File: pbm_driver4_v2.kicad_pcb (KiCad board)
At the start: 4 copper layers, 30 x 70 mm, 90 parts, among them J1 Conn_02x10_Odd_Even, J2 Conn_01x10, J3 Conn_01x02, J4 Conn_01x02, Q1 PSMN4R0-30YLDX, Q2 PSMN4R0-30YLDX, Q3 PSMN4R0-30YLDX, Q4 PSMN4R0-30YLDX, U11 TS5A3159ADCK, U12 TS5A3159ADCK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

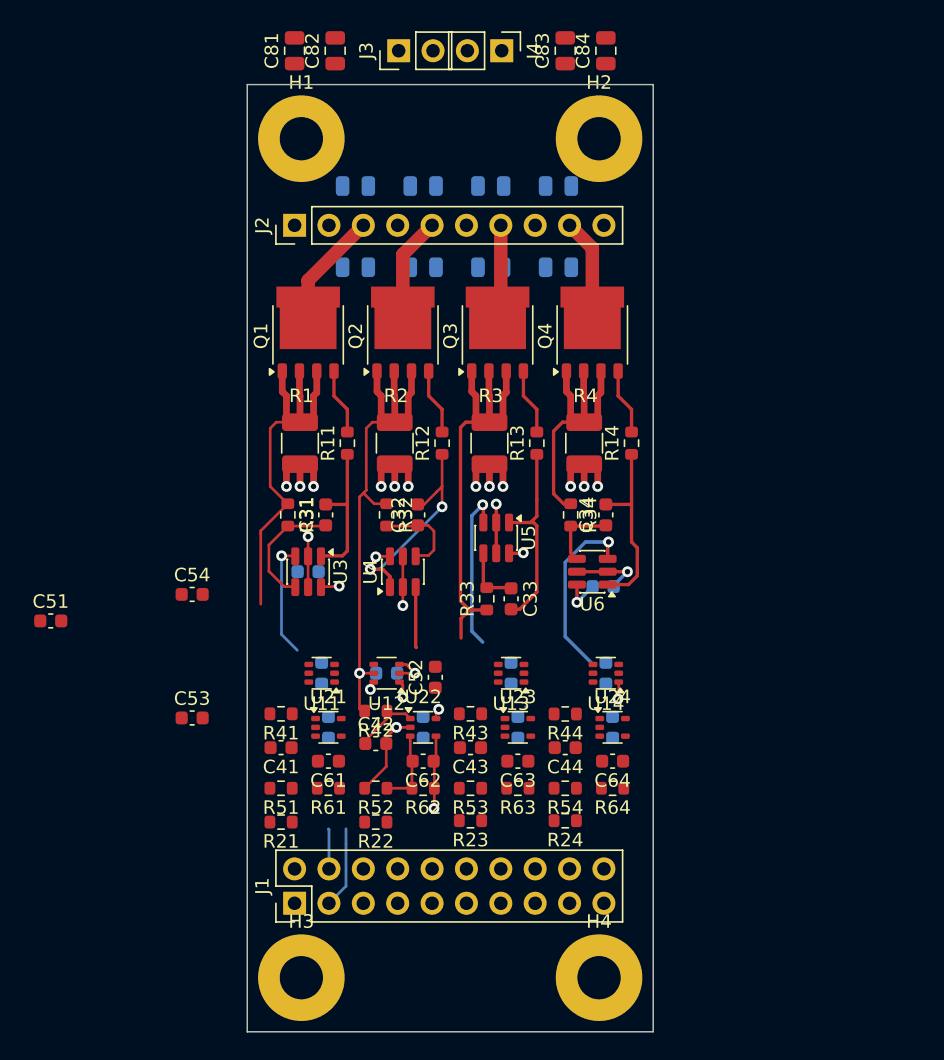
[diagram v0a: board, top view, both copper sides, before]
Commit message: Added pull-downs to output of Sense filter op amps
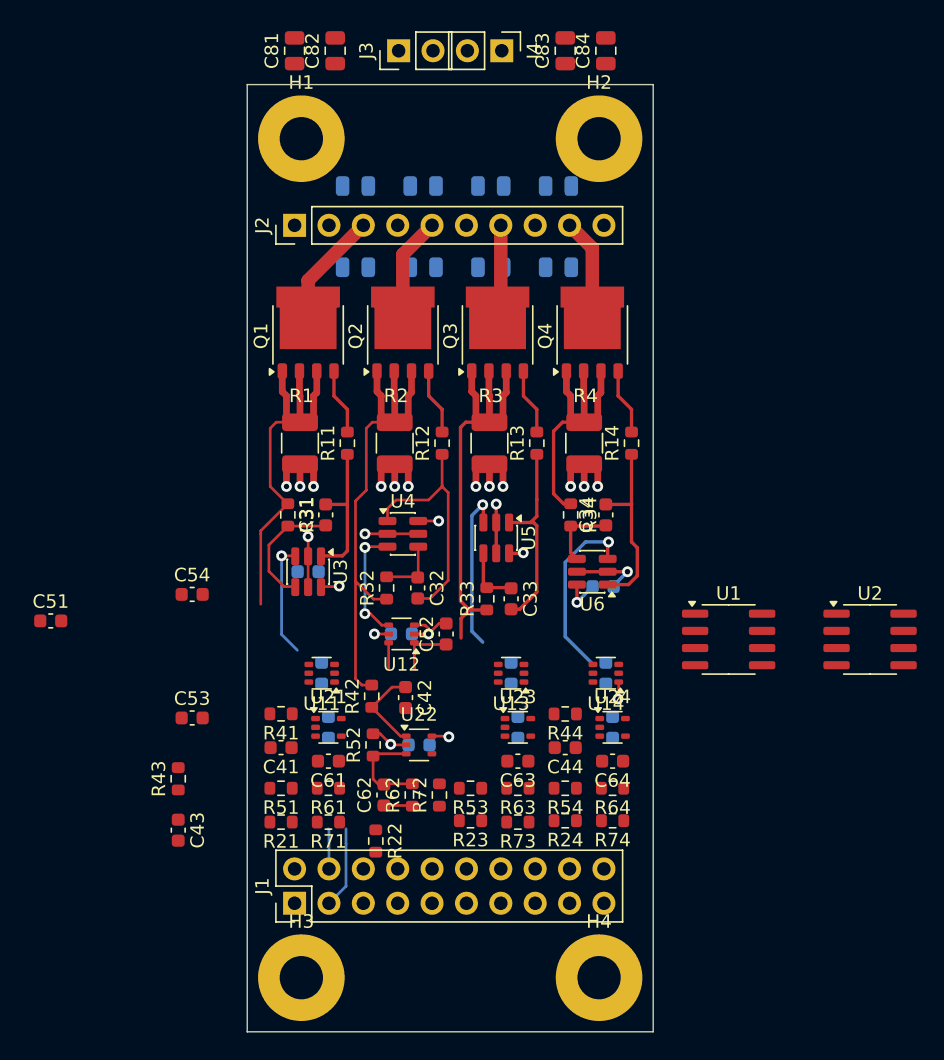
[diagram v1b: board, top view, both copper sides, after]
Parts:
- added R71: 10K 1%, $Local:R_0603_1608Metric, F.Cu at (6.00, -15.5)
- added R72: 10K 1%, $Local:R_0603_1608Metric, F.Cu at (14.2, -17.5)
- added R73: 10K 1%, $Local:R_0603_1608Metric, F.Cu at (20.0, -15.5)
- added R74: 10K 1%, $Local:R_0603_1608Metric, F.Cu at (27.0, -15.6)
- added U1: ADA4099-2xR, $Local:SOIC-8_3.9x4.9mm_P1.27mm, F.Cu at (35.6, -29.0)
- added U2: ADA4099-2xR, $Local:SOIC-8_3.9x4.9mm_P1.27mm, F.Cu at (46.0, -29.0)
- moved C43 22.4 mm to (-5.10, -14.9), turned to -90 degrees
- moved R43 22.1 mm to (-5.10, -18.7), turned to 90 degrees
- moved C32 5.40 mm to (12.6, -32.8), turned to -90 degrees
- moved R32 5.40 mm to (10.3, -32.8), turned to 90 degrees
- moved C42 4.05 mm to (11.7, -24.7), turned to -90 degrees
- moved C62 3.83 mm to (10.1, -17.5), turned to 90 degrees
- moved C52 3.30 mm to (14.7, -29.4)
- moved R52 3.21 mm to (9.30, -21.2), turned to 90 degrees
- moved C12 3.10 mm to (11.4, -29.4)
- moved U12 3.10 mm to (11.4, -29.4)
- moved U4 2.80 mm to (11.5, -36.8), turned to 0 degrees
- moved R22 1.40 mm to (9.50, -14.1), turned to -90 degrees
- moved C22 1.33 mm to (12.7, -21.2), turned to 180 degrees
- moved U22 1.33 mm to (12.7, -21.2)
- moved R42 1.14 mm to (9.20, -24.8), turned to 90 degrees
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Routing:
- net /Driver2/REF: track 4.48 -> 8.79 mm, vias 0 -> 2
- net /DAC2: track 5.47 -> 8.62 mm, vias 2 -> 1
- net /SENSE2: track 5.45 -> 2.52 mm, vias 1 -> 0
- net /Driver2/FB: track 6.64 -> 4.56 mm
- net /Driver2/OUT: track 15.9 -> 17.9 mm, vias 2 -> 0
- net GND: track 45.7 -> 44.0 mm
- net /Driver2/FILTER: track 5.03 -> 6.55 mm
- net /Driver2/FILTER_FB: track 5.79 -> 7.31 mm
- net /SEL2: track 0.90 -> 1.90 mm, vias 1 -> 0

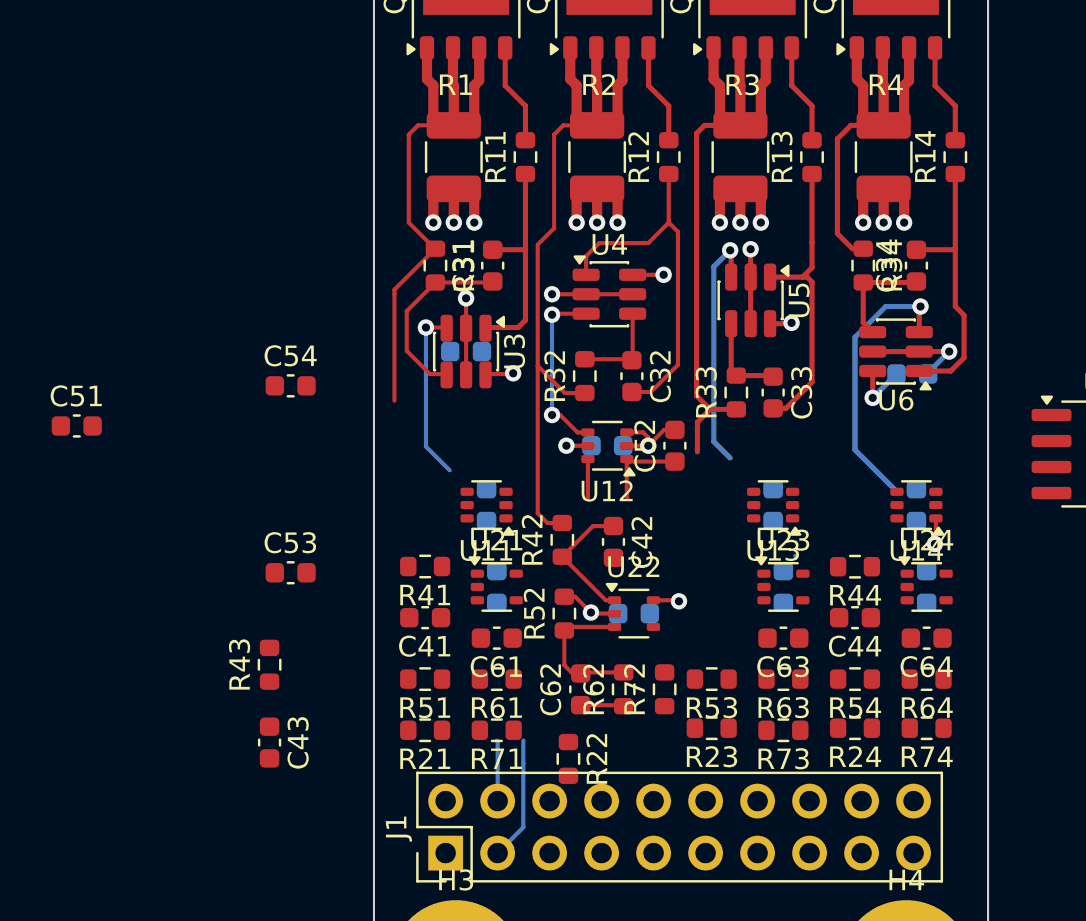
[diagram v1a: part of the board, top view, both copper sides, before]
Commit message: WIP routing and placement with OPA365
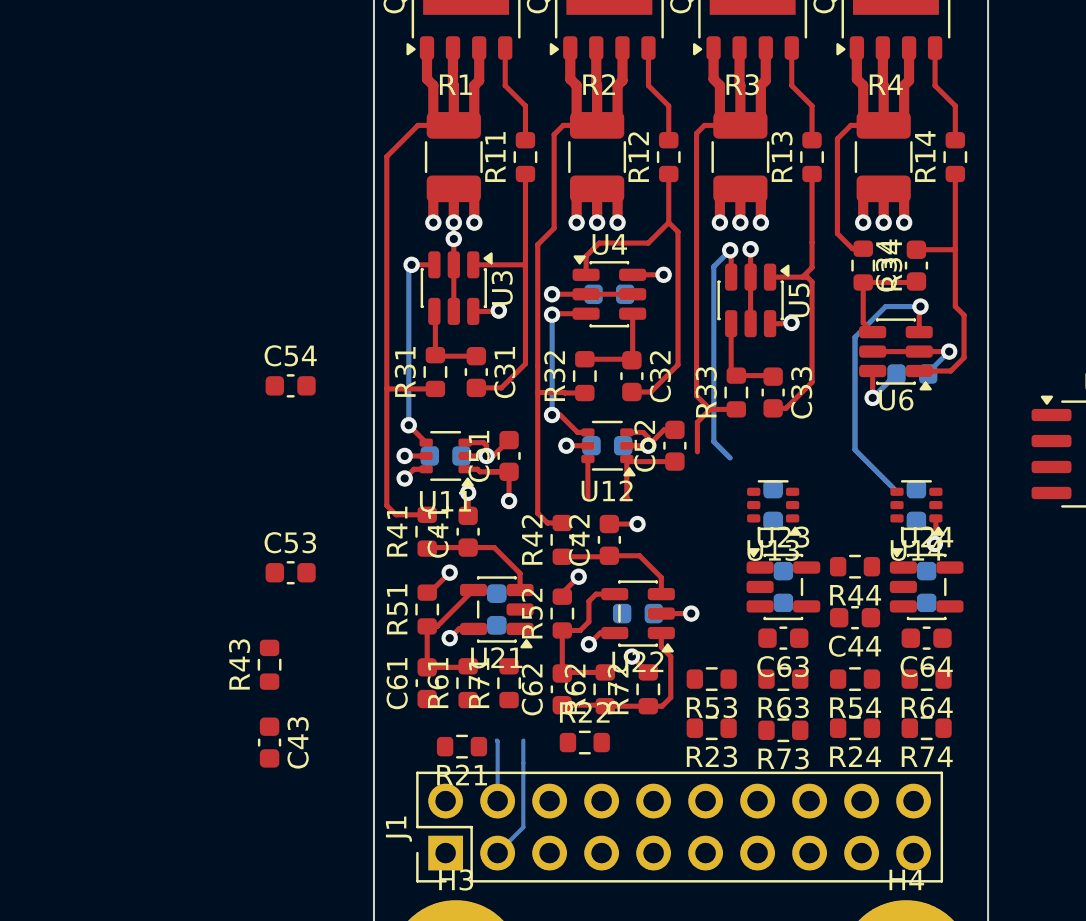
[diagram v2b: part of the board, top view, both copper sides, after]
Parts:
- U21, U22, U23, U24: value OPA333 -> OPA365AIDBV; footprint Package_TO_SOT_SMD:SOT-353_SC-70-5 -> $Local:SOT-23-5
- U3, U4, U5, U6: value ADA4099-2xR -> ADA4099-1; footprint Package_TO_SOT_SMD:TSOT-23-6 -> $Local:TSOT-23-6
- moved C51 21.2 mm to (6.60, -28.9), turned to 90 degrees
- moved C1 7.54 mm to (11.5, -36.8)
- moved C31 5.26 mm to (5.00, -33.0), turned to -90 degrees
- moved R31 5.20 mm to (3.00, -33.0), turned to 90 degrees
- moved C41 4.70 mm to (4.60, -25.2), turned to 90 degrees
- moved C61 4.05 mm to (2.60, -17.8), turned to 90 degrees
- moved R51 3.40 mm to (2.60, -21.4), turned to 90 degrees
- moved U3 3.16 mm to (3.90, -37.1)
- moved C11 3.12 mm to (3.50, -28.9), turned to 180 degrees
- moved U11 3.12 mm to (3.50, -28.9)
- moved R71 2.38 mm to (6.60, -17.8), turned to 90 degrees
- moved R21 1.97 mm to (4.30, -14.7)
- moved R41 1.70 mm to (2.60, -25.2), turned to 90 degrees
- moved R61 1.41 mm to (4.60, -17.8), turned to 90 degrees
- moved R22 1.13 mm to (10.3, -14.9), turned to 0 degrees
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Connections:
- U21 pad 1: /Driver1/FILTER -> /SENSE1
- U21 pad 3: /Driver1/FILTER_FB -> /Driver1/FILTER
- U21 pad 4: /SENSE1 -> /Driver1/FILTER_FB
- U22 pad 1: /Driver2/FILTER -> /SENSE2
- U22 pad 3: /Driver2/FILTER_FB -> /Driver2/FILTER
- U22 pad 4: /SENSE2 -> /Driver2/FILTER_FB
- U23 pad 1: /Driver3/FILTER -> /SENSE3
- U23 pad 3: /Driver3/FILTER_FB -> /Driver3/FILTER
- U23 pad 4: /SENSE3 -> /Driver3/FILTER_FB
- U24 pad 1: /Driver4/FILTER -> /SENSE4
- U24 pad 3: /Driver4/FILTER_FB -> /Driver4/FILTER
- U24 pad 4: /SENSE4 -> /Driver4/FILTER_FB
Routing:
- net GND: track 44.0 -> 53.0 mm, vias 18 -> 24
- net /Driver1/SENSE_R: track 30.3 -> 39.0 mm
- net /Driver1/FILTER_FB: track 0.00 -> 7.02 mm
- net /SENSE2: track 2.52 -> 8.84 mm
- net /Driver1/FILTER: track 0.00 -> 5.89 mm
- net /Driver1/FB: track 9.16 -> 4.28 mm
- net /DAC1: track 6.06 -> 10.8 mm, vias 0 -> 1
- net /Driver1/OUT: track 10.8 -> 14.6 mm
- net +3.3V: track 2.32 -> 4.94 mm, vias 2 -> 4
- net /Driver1/REF: track 8.47 -> 10.3 mm, vias 1 -> 2
- net /SEL1: track 0.00 -> 1.24 mm, vias 0 -> 1
- net /Driver2/FILTER_FB: track 7.31 -> 8.10 mm
- net /Driver2/SENSE_R: track 38.9 -> 38.4 mm
- removed copper zone on In2.Cu, net +12V
- removed copper zone on In2.Cu, net +3.3V

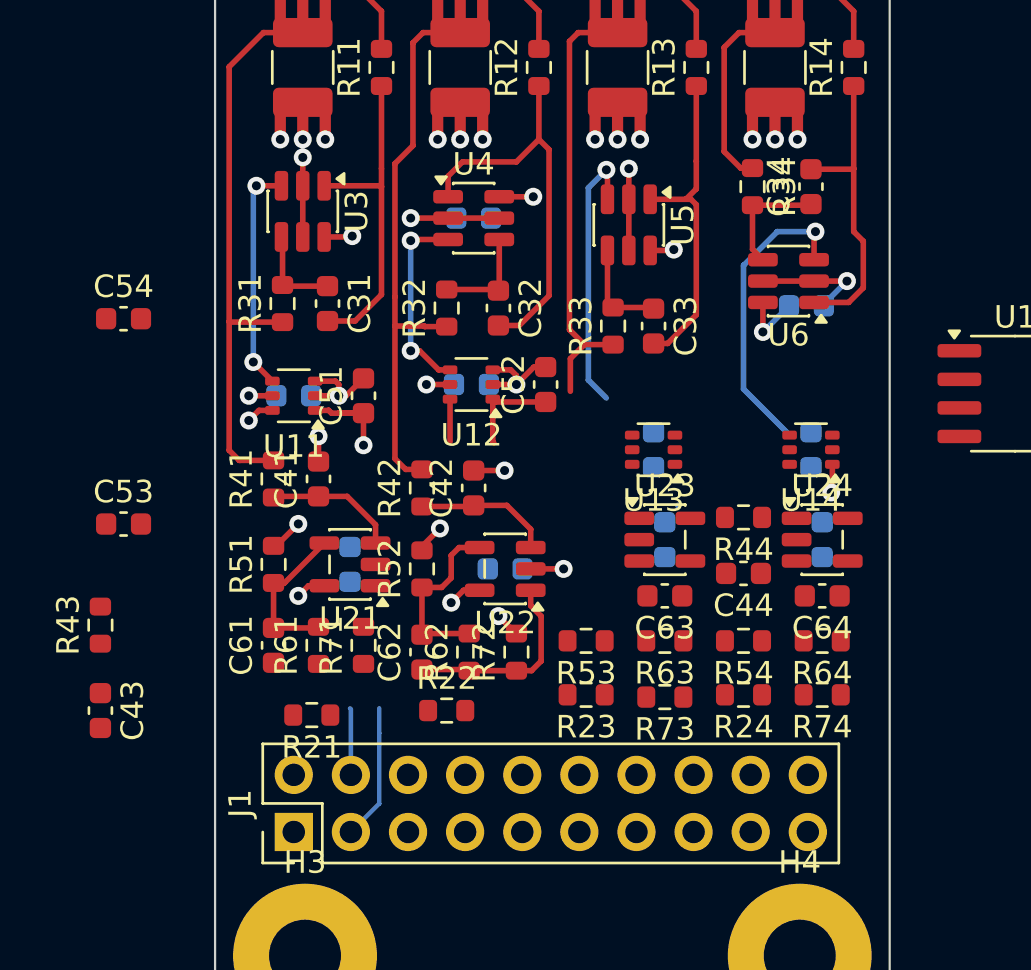
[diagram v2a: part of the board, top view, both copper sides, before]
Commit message: Top side only placement and routing figured out (Channel 1).
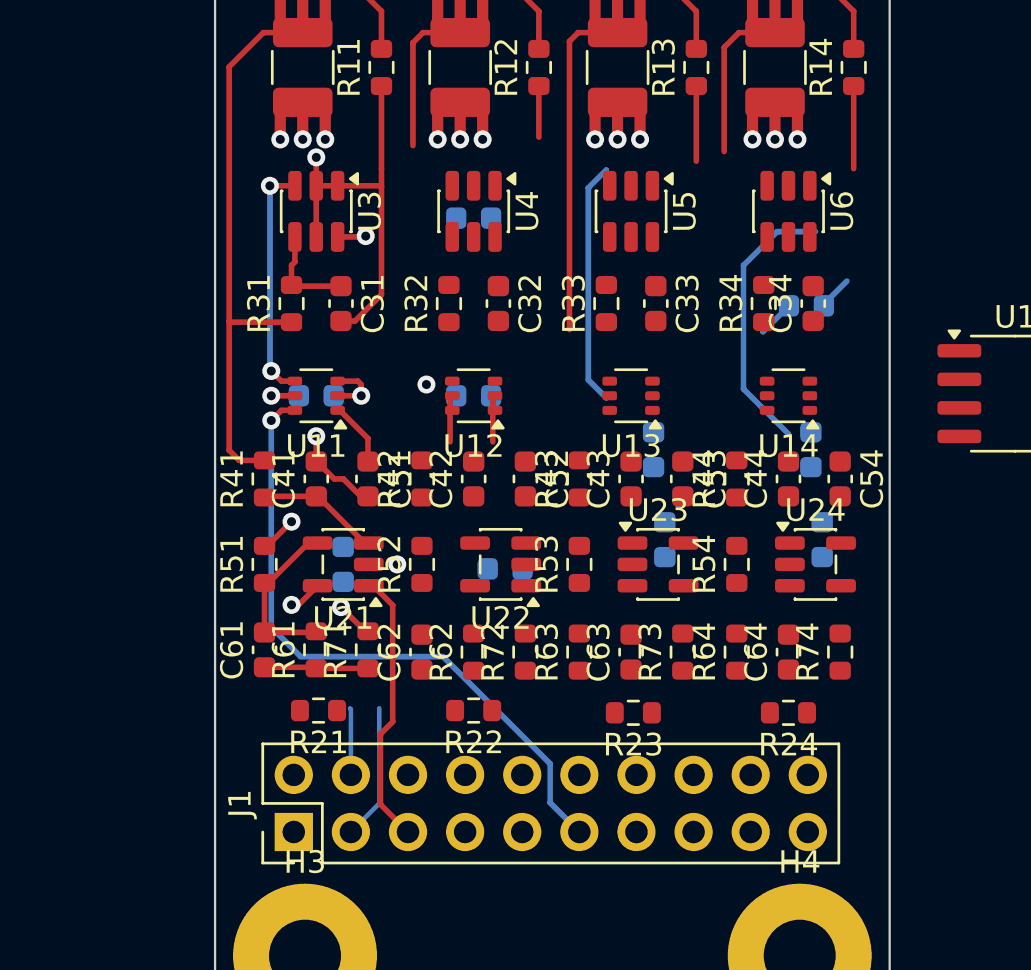
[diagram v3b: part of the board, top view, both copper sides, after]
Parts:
- moved C54 32.7 mm to (27.8, -25.2), turned to -90 degrees
- moved C43 25.7 mm to (18.5, -25.2), turned to 90 degrees
- moved C53 25.0 mm to (20.8, -25.2), turned to -90 degrees
- moved R43 22.3 mm to (16.2, -25.2)
- moved R34 5.22 mm to (24.4, -33.0), turned to 90 degrees
- moved C34 5.20 mm to (26.6, -33.0)
- moved C44 4.65 mm to (25.5, -25.2), turned to 90 degrees
- moved C52 4.30 mm to (13.8, -25.2), turned to -90 degrees
- moved R63 3.83 mm to (16.2, -17.5), turned to 90 degrees
- moved R64 3.83 mm to (23.2, -17.5), turned to 90 degrees
- moved C51 3.71 mm to (6.80, -25.2), turned to -90 degrees
- moved R53 3.41 mm to (16.2, -21.4), turned to 90 degrees
- moved R54 3.41 mm to (23.2, -21.4), turned to 90 degrees
- moved U6 3.10 mm to (25.5, -37.1), turned to -90 degrees
- moved C63 2.92 mm to (18.5, -17.5), turned to 90 degrees
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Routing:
- net /SEL1: track 1.24 -> 28.9 mm
- net GND: track 53.0 -> 34.9 mm, vias 24 -> 18
- net /Driver2/SENSE_R: track 38.4 -> 20.4 mm
- net /SENSE1: track 0.00 -> 16.7 mm
- net /Driver2/OUT: track 17.9 -> 2.27 mm
- net /Driver3/OUT: track 14.7 -> 3.34 mm
- net /Driver4/OUT: track 13.5 -> 3.67 mm
- net /SENSE2: track 8.84 -> 0.00 mm
- net /Driver2/REF: track 8.79 -> 0.00 mm, vias 2 -> 0
- net /Driver2/FILTER_FB: track 8.10 -> 0.00 mm
- net /Driver2/FILTER: track 6.11 -> 0.00 mm
- net /Driver4/FB: track 5.24 -> 0.00 mm
- net /Driver2/FB: track 4.56 -> 0.00 mm
- net /Driver3/SENSE_R: track 33.2 -> 28.6 mm
- net /Driver3/FB: track 4.46 -> 0.00 mm
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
